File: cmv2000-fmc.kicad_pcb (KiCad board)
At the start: 4 copper layers, 70 x 35 mm, 75 parts, among them J1 Conn_01x02, J10 LVDS_CTR_P, J11 LVDS_CTR_N, J12 LVDS_1_P, J13 LVDS_1_N, J14 LVDS_2_P, J15 LVDS_2_N, J2 Conn_02x05, J3 LVDS_CLK_IN_P, J4 LVDS_CLK_IN_N, J5 LVDS_CLK_OUT_P, J6 LVDS_CLK_OUT_N, J7 CLK_IN, J8 CLK_IN, J9 Conn_01x02, P1 FMC_LPC, P2 CONN_41, P3 CONN_51, Q1 Q_NMOS_GSD, U1 AP3211, U2 SN74AXC8T245, U3 BD49xxx_GND1, U4 SN74LVC2T45

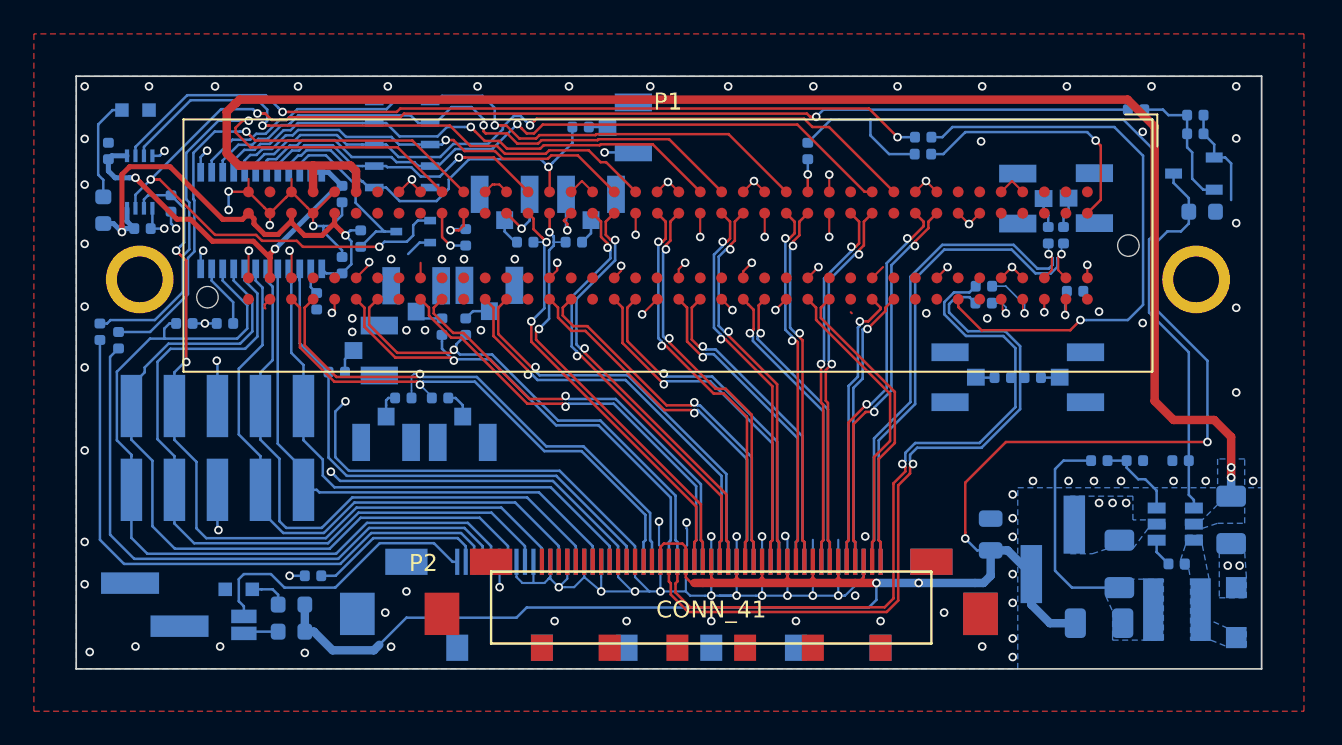
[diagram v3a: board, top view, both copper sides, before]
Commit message: replace custom Hirose U.FL-R-SMT-1 footprint by upstream one
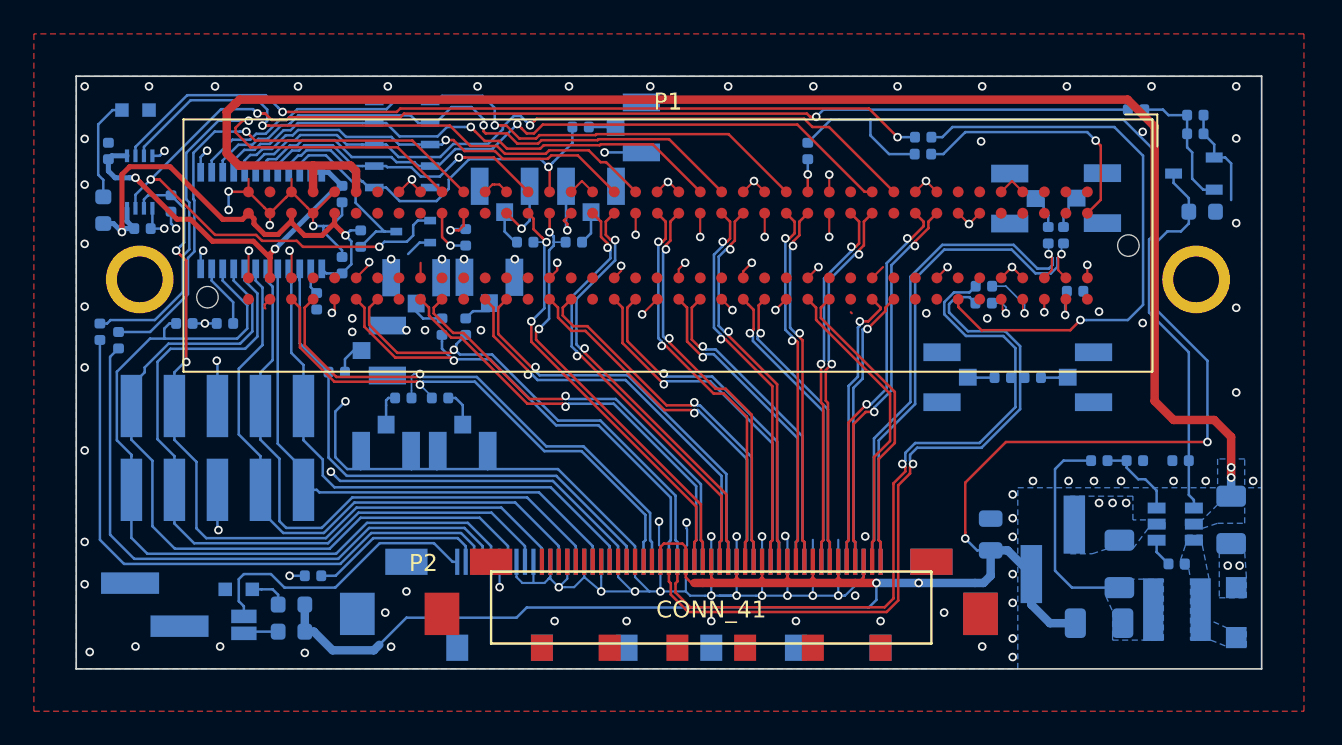
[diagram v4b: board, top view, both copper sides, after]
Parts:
- J10, J11, J12, J13, J14, J15, J3, J4, J5, J6, J7, J8: footprint footprints:U.FL-R-SMT-1 -> Connector_Coaxial:U.FL_Hirose_U.FL-R-SMT-1_Vertical
- turned J10 to 270 degrees
- turned J11 to 270 degrees
- turned J12 to 90 degrees
- turned J13 to 90 degrees
- turned J14 to 90 degrees
- turned J15 to 90 degrees
- turned J3 to 180 degrees
- turned J4 to 0 degrees
- turned J5 to 0 degrees
- turned J6 to 180 degrees
- turned J7 to 0 degrees
- turned J8 to 0 degrees
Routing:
- net GND: track 199.3 -> 203.8 mm
